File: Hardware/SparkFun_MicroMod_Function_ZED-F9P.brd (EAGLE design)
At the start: 38 x 65 mm, 56 parts, among them J2 MICROMOD_STANDARD, J3 QWIIC_RA, U1 EEPROM, U2 PCA9306DCUR, U3 U-BLOX_ZED-F9P, U4 74LVC541ABQ, U5 74LVC541ABQ, U6 SN74AUP1T04DCK

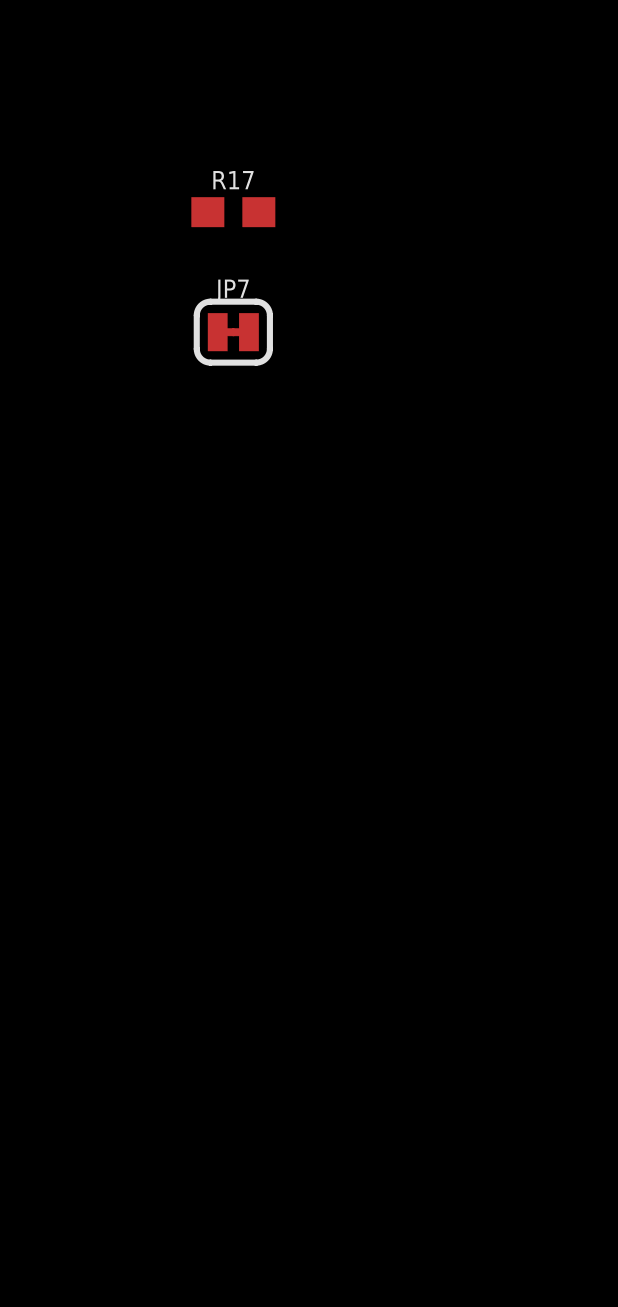
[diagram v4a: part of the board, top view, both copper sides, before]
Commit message: Added I/O and passives. Changed net names.
Added passives surrounding IC's.
Modified names to be more descriptive.
Reorganized schematic for visual representation.
Added Descriptions of schematic symbols.
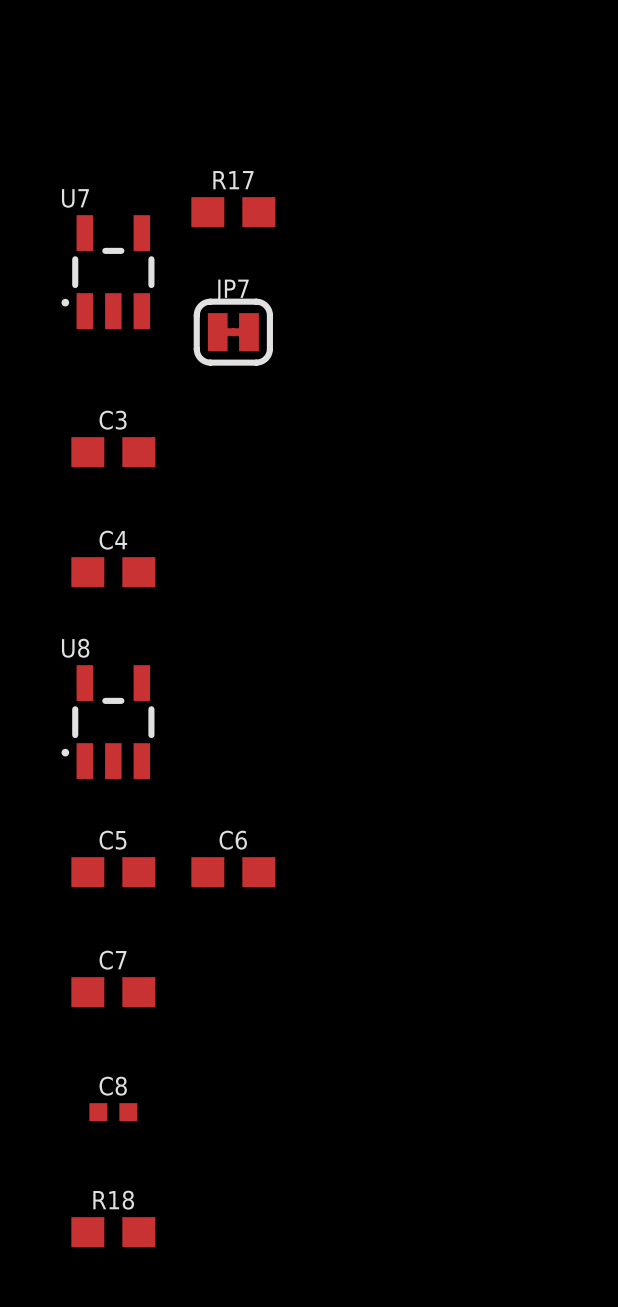
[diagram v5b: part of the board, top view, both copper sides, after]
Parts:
- added C3, C5: 470pF, SparkFun-Capacitors:0603
- added C4, C6: 2.2uF, SparkFun-Capacitors:0603
- added C7: 1.0uF, SparkFun-Capacitors:0603
- added C8: 0.1uF, SparkFun-Capacitors:0402-TIGHT
- added R18: 100k, SparkFun-Resistors:0603
- added U7, U8: MIC5219 3.3V, SparkFun-IC-Power:SOT23-5
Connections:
- removed net N$16: JP7.2
- removed net N$19: J2.47
- removed net N$39: U4.P$20
- removed net N$42: U5.P$20
- removed net N$69: U3.38
- removed net N$77: U3.33, U3.34
- new net N$17: C3.1, U7.4
- new net VDD: C4.1, JP7.2, R12.2, R13.2, R14.2, U3.33, U3.34, U4.P$20, U5.P$20, U6.P$2, U6.P$5, U7.5
- new net V_USB_2: C6.1, C7.1, C8.1, R18.2, U3.38, U8.5
- net 3.3V: no longer R12.2, R13.2, R14.2
- net EXTINT: now also J2.23
- net GND: now also C3.2, C4.2, C5.2, C6.2, C7.2, C8.2, R18.1, U7.2, U8.2
- net N$14: now also C5.1, U8.4; no longer U6.P$2, U6.P$5
- net TX_READY: now also J2.47; no longer J2.23
- net VCC: now also U7.1, U7.3
- net V_USB: now also U8.1, U8.3

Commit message: Completed antenna supervisor. Started External Antenna Power.
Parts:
- removed U3: U-BLOX_ZED-F9P, MicroMod_Function_GNSS_ublox_ZED-F9P:ZED-F9P
- added BYP, USB_EN: JUMPER-SMT_2_NO_SILK, SparkFun-Jumpers:SMT-JUMPER_2_NO_SILK
- added C10, C11, C14: 0.1uF, SparkFun-Capacitors:0402
- added C12: GRM0335C1H470JA01, MicroMod_Function_GNSS_ublox_ZED_F9P:0201_CAP
- added C13: 10nF, SparkFun-Capacitors:0402-TIGHT
- added C9: 0402YD104JAT2A, MicroMod_Function_GNSS_ublox_ZED_F9P:0402_MURATA
- added D10, D9: 3A/10V/280mV, SparkFun-DiscreteSemi:SOD-323
- added D11, D12, D8: RED, SparkFun-LED:LED-0603
- added D13: PESD0402, SparkFun-DiscreteSemi:0402
- added F1: 6V/2A, SparkFun-Fuses:1210
- added FB1: BLM18AG102BH1D, MicroMod_Function_GNSS_ublox_ZED_F9P:0603_MURATA
- added J4: U.FL, SparkFun-RF:SMA-EDGE
- added JP10, JP8, JP9: JUMPER-SMT_2_NC_TRACE_SILK, SparkFun-Jumpers:SMT-JUMPER_2_NC_TRACE_SILK
- added JP11, JP12: (no value), SparkFun-Jumpers:SMT-JUMPER_3_2-NC_TRACE_SILK
- added L1, L2: LQW15ANR12J00D, MicroMod_Function_GNSS_ublox_ZED_F9P:0402_MURATA
- added Q1: DMP21D0UT, MicroMod_Function_GNSS_ublox_ZED_F9P:SOT523
- added Q2, Q3: 600mA/40V, SparkFun-DiscreteSemi:SOT23-3
- added R19, R20, R21, R23: 1k, SparkFun-Resistors:0603
- added R22, R26: CRGP2010F10R, MicroMod_Function_GNSS_ublox_ZED_F9P:2010
- added R24, R25: 100k, SparkFun-Resistors:0603
- added R27: 220, SparkFun-Resistors:0603
- added R28: 2.2k, SparkFun-Resistors:0603
- added U$3: OPA344, SparkFun-IC-Amplifiers:SOT23-5
- added U9: 74LVC541ABQ, MicroMod_Function_GNSS_ublox_ZED_F9P:DHVQFN20
- JP7: value NC -> JUMPER-SMT_2_NO_SILK; device SparkFun-Jumpers:SMT-JUMPER_2_NC_TRACE_SILK -> SparkFun-Jumpers:SMT-JUMPER_2_NO_SILK
- R17: value 10k -> 100k
- U2: value PCA9306DCUR -> U-BLOX_ZED-F9P; device MicroMod_Function_GNSS_ublox_ZED-F9P:VSSOP-8_DCU -> MicroMod_Function_GNSS_ublox_ZED_F9P:ZED-F9P
- U4: value 74LVC541ABQ -> SN74AUP1T04DCK; device MicroMod_Function_GNSS_ublox_ZED-F9P:DHVQFN20 -> MicroMod_Function_GNSS_ublox_ZED_F9P:SC-70-5_DCK
- U5: value 74LVC541ABQ -> PCA9306DCUR; device MicroMod_Function_GNSS_ublox_ZED-F9P:DHVQFN20 -> MicroMod_Function_GNSS_ublox_ZED_F9P:VSSOP-8_DCU
- U6: value SN74AUP1T04DCK -> 74LVC541ABQ; device MicroMod_Function_GNSS_ublox_ZED-F9P:SC-70-5_DCK -> MicroMod_Function_GNSS_ublox_ZED_F9P:DHVQFN20
- moved U2 547.3 mm to (-44.0, -886.0)
- moved R1 467.3 mm to (-0.85, -612.7)
- moved R3 467.3 mm to (-0.85, -676.2)
- moved R2 467.2 mm to (-0.85, -625.4)
- moved R4 467.2 mm to (-0.85, -663.5)
- moved R5 467.2 mm to (-0.85, -688.9)
- moved R6 467.2 mm to (-0.85, -701.6)
- moved R8 467.2 mm to (-0.85, -638.1)
- moved R11 467.2 mm to (-0.85, -650.8)
- moved R7 467.2 mm to (-0.85, -714.3)
- moved C7 460.6 mm to (-54.0, -898.0)
- moved C8 456.2 mm to (-46.0, -898.0)
- moved R18 452.4 mm to (-50.0, -898.0)
- moved R17 404.7 mm to (-0.85, -815.9)
- moved R16 394.2 mm to (-0.85, -777.8)
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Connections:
- removed net !SHORT!: U4.P$8
- removed net N$73: U3.7
- removed net N$74: U3.2
- removed net TIMEPULSE: U5.P$12
- removed net ZED_!ANT_SHORT!: U3.6
- removed net ZED_!SHORT!: U4.P$12
- removed net ZED_TIMEPULSE: U3.53, U5.P$8
- new net ANT_!SHORT!: Q1.P$1, R22.2, R23.2, U6.P$8
- new net GND2: JP10.2, JP2.2, JP3.2, JP4.1, JP5.1, JP6.1, JP8.2, JP9.2
- new net GND_RF: C13.2, C14.1, C3.2, C4.2, C5.2, C6.2, C7.2, C8.2, C9.P$2, D13.1, J4.GND@0, J4.GND@1, J4.GND@2, J4.GND@3, R18.1, R24.1, R28.1, U$3.2, U2.1, U2.100, U2.101, U2.102, U2.12, U2.14, U2.3, U2.32, U2.37, U2.41, U2.48, U2.55, U2.56, U2.57, U2.58, U2.59, U2.60, U2.61, U2.62, U2.63, U2.64, U2.65, U2.66, U2.67, U2.68, U2.69, U2.70, U2.71, U2.72, U2.73, U2.74, U2.75, U2.76, U2.77, U2.78, U2.79, U2.80, U2.81, U2.82, U2.83, U2.84, U2.85, U2.86, U2.87, U2.88, U2.89, U2.90, U2.91, U2.92, U2.93, U2.94, U2.95, U2.96, U2.97, U2.98, U2.99
- new net N$15: JP8.1, R19.1
- new net N$16: D8.C, R19.2
- new net N$19: D10.A, USB_EN.2
- new net N$20: BYP.1, D10.C, D9.C, F1.1
- new net N$39: JP10.1, R21.1
- new net N$40: D12.C, R21.2
- new net N$41: C9.P$1, L2.P$2, Q3.3
- new net N$42: JP12.1, R14.2
- new net N$43: JP11.1, R15.2
- new net N$44: JP11.3, R16.2
- new net N$47: JP12.3, R13.2
- new net N$48: R23.1, R24.2, U$3.3
- new net N$49: C13.1, L1.P$2, R22.1, U$3.4
- new net N$50: Q2.1, Q3.2, R26.1
- new net N$51: Q2.3, Q3.1, R28.2
- new net N$52: Q2.2, R27.1
- new net N$53: FB1.P$2, R26.2, R27.2
- new net RF_IN: C12.P$2, U2.2
- new net SMA_RF_IN: C12.P$1, D13.2, J4.SIG, L1.P$1, L2.P$1
- new net V_RF: C14.2, Q1.P$2, R25.1, U$3.5, U2.7
- new net ZED_ANT_!SHORT!: U2.6, U6.P$12
- new net ZED_PPS: U2.53, U9.P$8
- net !RESET!: now also U6.P$4; no longer U4.P$4
- net !SAFEBOOT!: now also U6.P$5; no longer U4.P$5
- net 3.3V: now also JP11.2, U5.P$2; no longer R15.2, R16.2, U2.P$2
- net ANT_DETECT: now also U$3.1, U6.P$7; no longer U4.P$7
- net ANT_OFF: now also Q1.P$3, R25.2, U9.P$18; no longer U5.P$18
- net EXTINT: now also U6.P$6; no longer U4.P$6
- net GEO_STAT: now also U9.P$17; no longer U5.P$17
- net GND: now also C10.2, C11.2, JP7.1, U4.P$3, U5.P$1, U6.P$10, U6.P$21, U9.P$10, U9.P$11, U9.P$21, U9.P$9; no longer C3.2, C4.2, C5.2, C6.2, C7.2, C8.2, JP2.2, JP3.2, JP4.1, JP5.1, JP6.1, R17.1, R18.1, U2.P$1, U3.1, U3.100, U3.101, U3.102, U3.12, U3.14, U3.3, U3.32, U3.37, U3.41, U3.48, U3.55, U3.56, U3.57, U3.58, U3.59, U3.60, U3.61, U3.62, U3.63, U3.64, U3.65, U3.66, U3.67, U3.68, U3.69, U3.70, U3.71, U3.72, U3.73, U3.74, U3.75, U3.76, U3.77, U3.78, U3.79, U3.80, U3.81, U3.82, U3.83, U3.84, U3.85, U3.86, U3.87, U3.88, U3.89, U3.90, U3.91, U3.92, U3.93, U3.94, U3.95, U3.96, U3.97, U3.98, U3.99, U4.P$10, U4.P$21, U5.P$10, U5.P$11, U5.P$21, U5.P$9, U6.P$3
- net IO_!OE!: now also U4.P$4, U6.P$1, U6.P$19, U9.P$1, U9.P$19; no longer U4.P$1, U4.P$19, U5.P$1, U5.P$19, U6.P$4
- net N$12: now also U5.P$7, U5.P$8; no longer U2.P$7, U2.P$8
- net N$24: now also JP7.2, R17.1, U6.P$9; no longer JP7.1, R17.2, U4.P$9
- net N$26: now also JP9.1, R20.1; no longer J2.59
- net N$30: now also D11.C, R20.2; no longer J2.61
- net PPS: now also U9.P$12
- net RTK_STAT: now also U9.P$16; no longer U5.P$16
- net RX/COPI: now also U6.P$3; no longer U4.P$3
- net RX2/RTCM: now also J2.61, U6.P$2; no longer U4.P$2
- net SCL/SCK: now also U5.P$3; no longer U2.P$3
- net SDA/!CS!: now also U5.P$4; no longer U2.P$4
- net TX/CIPO: now also U9.P$14; no longer U5.P$14
- net TX2/RTCM: now also J2.59, U9.P$15; no longer U5.P$15
- net TX_READY: now also U9.P$13; no longer U5.P$13
- net VCC: now also BYP.2, F1.2; no longer J2.72, J2.74
- net VDD: now also C10.1, C11.1, D11.A, JP12.2, R17.2, U2.33, U2.34, U4.P$2, U4.P$5, U6.P$20, U8.3, U9.P$20; no longer JP7.2, R13.2, R14.2, U3.33, U3.34, U4.P$20, U5.P$20, U6.P$2, U6.P$5
- net VIN: now also D9.A, J2.72, J2.74
- net V_BATT: now also U2.36; no longer U3.36
- net V_USB: now also D8.A, USB_EN.1; no longer U8.3
- net V_USB_2: now also D12.A, U2.38; no longer U3.38
- net ZED_!RESET!: now also U2.49, U6.P$16; no longer U3.49, U4.P$16
- net ZED_!SAFEBOOT!: now also U2.50, U6.P$15; no longer U3.50, U4.P$15
- net ZED_ANT_DETECT: now also U2.4, U6.P$13; no longer U3.4, U4.P$13
- net ZED_ANT_OFF: now also U2.5, U9.P$2; no longer U3.5, U5.P$2
- net ZED_DSEL: now also U2.47, U6.P$11; no longer U3.47, U4.P$11
- net ZED_EXTINT: now also U2.51, U6.P$14; no longer U3.51, U4.P$14
- net ZED_GEO_STAT: now also U2.19, U9.P$3; no longer U3.19, U5.P$3
- net ZED_RTK_STAT: now also U2.20, U9.P$4; no longer U3.20, U5.P$4
- net ZED_RX/COPI: now also U2.43, U6.P$17; no longer U3.43, U4.P$17
- net ZED_RX2/RTCM: now also U2.26, U6.P$18; no longer U3.26, U4.P$18
- net ZED_SCL/SCK: now also U2.45, U5.P$6; no longer U2.P$6, U3.45
- net ZED_SDA/!CS!: now also U2.44, U5.P$5; no longer U2.P$5, U3.44
- net ZED_TX/CIPO: now also U2.42, U9.P$6; no longer U3.42, U5.P$6
- net ZED_TX2/RTCM: now also U2.27, U9.P$5; no longer U3.27, U5.P$5
- net ZED_TX_READY: now also U2.46, U9.P$7; no longer U3.46, U5.P$7
- net ZED_USB_N: no longer U3.39
- net ZED_USB_P: no longer U3.40
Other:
- board text added: "4-Layer"
- board text removed: "2-Layer"

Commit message: Commit for current progress.
Committing so others can begin a schematic review while I finish up.
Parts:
- removed C12: GRM0335C1H470JA01, MicroMod_Function_GNSS_ublox_ZED_F9P:0201_CAP
- added C15: CBR04C470J5GAC, MicroMod_Function_GNSS_ublox_ZED_F9P:0402-TIGHT
- added J5: (no value), SparkFun-Connectors:1X02_XTRA_BIG
- L1: value LQW15ANR12J00D -> LQW18ANR12J8ZD; device MicroMod_Function_GNSS_ublox_ZED_F9P:0402_MURATA -> MicroMod_Function_GNSS_ublox_ZED_F9P:0603_MURATA
- moved L1 345.0 mm to (-55.0, -917.0)
- moved FB1 16.6 mm to (-48.0, -913.0)
- moved L2 15.6 mm to (-45.0, -913.0)
- moved R27 14.8 mm to (-47.0, -908.0)
- moved R28 11.0 mm to (-54.0, -914.0)
- moved Q3 8.49 mm to (-47.0, -903.0)
- moved R26 7.00 mm to (-53.0, -909.0)
- moved C9 4.12 mm to (-51.0, -913.0)
- moved Q2 1.00 mm to (-53.0, -903.0)
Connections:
- new net SMA_RF_IN1: L2.P$1
- net RF_IN: now also C15.2; no longer C12.P$2
- net SMA_RF_IN: now also C15.1; no longer C12.P$1, L2.P$1
- net ZED_USB_N: now also U2.39
- net ZED_USB_P: now also U2.40

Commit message: Schematic V1.0
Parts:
- removed FB1: BLM18AG102BH1D, MicroMod_Function_GNSS_ublox_ZED_F9P:0603_MURATA
- removed L2: LQW15ANR12J00D, MicroMod_Function_GNSS_ublox_ZED_F9P:0402_MURATA
- removed Q2, Q3: 600mA/40V, SparkFun-DiscreteSemi:SOT23-3
- removed R27: 220, SparkFun-Resistors:0603
- removed R28: 2.2k, SparkFun-Resistors:0603
- added C12: 0.1uF, SparkFun-Capacitors:0402
- added C16, C17: 0.1uF, SparkFun-Capacitors:0603
- added J6, J7: (no value), SparkFun-Connectors:1X01
- added SUPPLY35: 2PT_GND_TIE, SparkFun-PowerSymbols:2PT_GND_TIE
- added TP1, TP10, TP11, TP12, TP13, TP14, TP15, TP16, TP17, TP18, TP19, TP2, TP20, TP3, TP4, TP5, TP6, TP8: TEST-POINT3, SparkFun-Connectors:PAD.03X.03
- added TP7, TP9: TEST-POINTPOGO_PTH, SparkFun-Connectors:1X01_NO_SILK
- added U$7: OPA344, SparkFun-IC-Amplifiers:SOT23-5
- added U3: FIN1017MXSOIC-8, MicroMod_Function_GNSS_ublox_ZED_F9P:SO08
- C9: value 0402YD104JAT2A -> 1.0uF; device MicroMod_Function_GNSS_ublox_ZED_F9P:0402_MURATA -> SparkFun-Capacitors:0603
- J5: device SparkFun-Connectors:1X02_XTRA_BIG -> SparkFun-Connectors:JST-2-SMD
- L1: value LQW18ANR12J8ZD -> LQW15AWR15J80D; device MicroMod_Function_GNSS_ublox_ZED_F9P:0603_MURATA -> MicroMod_Function_GNSS_ublox_ZED_F9P:0402_MURATA
- R22: value CRGP2010F10R -> 20; device MicroMod_Function_GNSS_ublox_ZED_F9P:2010 -> SparkFun-Resistors:0603
- R23: value 1k -> 2.0k
- R25: value 100k -> 10k
- R26: value CRGP2010F10R -> DNP; device MicroMod_Function_GNSS_ublox_ZED_F9P:2010 -> SparkFun-Resistors:0603_NO_CREAM
- moved C5 547.5 mm to (-54.0, -981.0)
- moved C13 369.2 mm to (-43.0, -961.0)
- moved D13 369.1 mm to (-47.0, -956.0)
- moved J4 369.0 mm to (-52.0, -952.0)
- moved R23 115.0 mm to (-54.0, -973.0)
- moved R22 100.0 mm to (-54.0, -969.0)
- moved Q1 99.0 mm to (-54.0, -964.0)
- moved R24 99.0 mm to (-54.0, -961.0)
- moved R25 87.1 mm to (-50.0, -961.0)
- moved J5 64.3 mm to (-63.0, -988.0)
- moved C9 64.1 mm to (-54.0, -977.0)
- moved R26 52.5 mm to (-46.0, -961.0)
- moved L1 49.0 mm to (-55.0, -966.0)
- moved C8 42.8 mm to (-38.0, -940.0)
- moved C7 42.0 mm to (-54.0, -940.0)
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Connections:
- removed net N$21: J2.51
- removed net N$22: J2.53
- removed net N$23: J2.55
- removed net N$25: J2.57
- removed net N$52: Q2.2, R27.1
- removed net N$53: FB1.P$2, R26.2, R27.2
- removed net SMA_RF_IN: C15.1, D13.2, J4.SIG, L1.P$1
- removed net SMA_RF_IN1: L2.P$1
- net !RESET!: now also J2.53, TP14.1
- net !SAFEBOOT!: now also J2.57, TP12.1
- net 3.3V: now also C16.1, TP8.1
- net ANT_!SHORT!: now also R22.1; no longer R22.2
- net ANT_DETECT: now also U$7.1; no longer U$3.1
- net ANT_OFF: now also R26.1
- net EXTINT: now also J2.55; no longer J2.23
- net GND: now also C12.2, C16.2, C17.1, C3.2, C5.2, SUPPLY35.P$2, TP1.1, TP2.1, TP7.1, U3.4
- net GND_RF: now also C9.2, D13.2, R25.1, SUPPLY35.P$1, TP4.1, TP9.1; no longer C3.2, C5.2, C9.P$2, D13.1, R28.1
- net N$41: now also C15.1, D13.1, J4.SIG, L1.P$2; no longer C9.P$1, L2.P$2, Q3.3
- net N$48: now also U$7.3; no longer U$3.3
- net N$49: now also L1.P$1, R22.2, U$7.4; no longer L1.P$2, R22.1, U$3.4
- net N$50: now also J5.1, U3.7; no longer Q2.1, Q3.2, R26.1
- net N$51: now also J5.2, U3.8; no longer Q2.3, Q3.1, R28.2
- net PPS: now also J2.51, TP13.1, U3.2
- net RX/COPI: now also TP15.1
- net RX2/RTCM: now also J6.1, TP17.1
- net SCL/SCK: now also TP19.1
- net SDA/!CS!: now also TP20.1
- net TX/CIPO: now also TP16.1
- net TX2/RTCM: now also J7.1, TP18.1
- net VCC: now also C12.1, TP6.1, U3.1
- net VDD: now also C14.2, C17.2, C9.1, TP3.1, U$3.5
- net V_BATT: now also TP5.1
- net V_RF: now also R26.2; no longer C14.2, R25.1, U$3.5
- net V_USB: now also TP10.1
- net V_USB_2: now also TP11.1
